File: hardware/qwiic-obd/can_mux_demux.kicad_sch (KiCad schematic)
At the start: 12 parts, among them Q201 2N7002, Q202 2N7002, Q203 2N7002, U201 TS5A3359DCUR, U202 TS5A3359DCUR, U203 TS5A3359DCUR

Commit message: Added initial layout (parts dump)
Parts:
- U201, U202, U203: footprint DCU8 -> UltraLibrarian:TS5A3359DCUR
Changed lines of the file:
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@@
       (effects (font (size 1.524 1.524)))
     )
-    (property "Footprint" "DCU8" (id 2) (at 105.41 125.984 0)
+    (property "Footprint" "UltraLibrarian:TS5A3359DCUR" (id 2) (at 105.41 125.984 0)
       (effects (font (size 1.524 1.524)) hide)
     )
@@
       (effects (font (size 1.524 1.524)))
     )
-    (property "Footprint" "DCU8" (id 2) (at 104.14 89.154 0)
+    (property "Footprint" "UltraLibrarian:TS5A3359DCUR" (id 2) (at 104.14 89.154 0)
       (effects (font (size 1.524 1.524)) hide)
     )
@@
       (effects (font (size 1.524 1.524)))
     )
-    (property "Footprint" "DCU8" (id 2) (at 104.14 54.864 0)
+    (property "Footprint" "UltraLibrarian:TS5A3359DCUR" (id 2) (at 104.14 54.864 0)
       (effects (font (size 1.524 1.524)) hide)
     )

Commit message: OK, layout v1 complete
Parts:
- added U202, U204: TS5A3359DCUR, UltraLibrarian:TS5A3359DCUR, symbol UltraLibrarian:TS5A3359DCUR
- renumbered U202 to U203, U203 to U205
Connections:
- net +5V: now also U202.8 (V+), U204.8 (V+)
- net CAN_SEL0: now also U202.6 (IN1), U204.6 (IN1)
- net CAN_SEL1: now also U202.5 (IN2), U204.5 (IN2)
- net GND: now also U202.4 (GND), U204.4 (GND)
- new net CAN_HI: U202.7 (COM)
- new net CAN_LO: U204.7 (COM)
- new net HS_CAN_HI: U202.1 (NO0)
- new net HS_CAN_LO: U204.1 (NO0)
- new net MS_CAN_HI: U202.2 (NO1)
- new net MS_CAN_LO: U204.2 (NO1)
- no-connect marks 1 -> 3
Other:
- moved on the sheet: Q201, Q202, Q203, R201, R202, R203, R204, R205, R206, U201, U203, U205

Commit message: Fix title block
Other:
- title: (none) -> QWIIC OBDII Interface
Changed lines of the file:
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@@
 (kicad_sch (version 20211123) (generator eeschema)
   (paper "A4")
+  (title_block
+    (title "QWIIC OBDII Interface")
+    (date "2023-01-03")
+  )
   (junction (at 140.97 135.89) (diameter 0) (color 0 0 0 0)
   )

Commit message: Shrunk layout a bit
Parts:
- U201, U202, U203, U204, U205: Digikey (none) -> 296-21193-1-ND
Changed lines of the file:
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@@
       (effects (font (size 1.524 1.524)))
+    )
+    (property "Digikey" "296-21193-1-ND" (id 4) (at 257.81 81.28 0)
+      (effects (font (size 1.27 1.27)) hide)
     )
     (pin "1")
@@
       (effects (font (size 1.524 1.524)))
     )
+    (property "Digikey" "296-21193-1-ND" (id 4) (at 257.81 115.57 0)
+      (effects (font (size 1.27 1.27)) hide)
+    )
     (pin "1")
     (pin "2")
@@
       (effects (font (size 1.524 1.524)))
     )
+    (property "Digikey" "296-21193-1-ND" (id 4) (at 99.06 135.89 0)
+      (effects (font (size 1.27 1.27)) hide)
+    )
     (pin "1")
     (pin "2")
@@
       (effects (font (size 1.524 1.524)))
     )
+    (property "Digikey" "296-21193-1-ND" (id 4) (at 97.79 99.06 0)
+      (effects (font (size 1.27 1.27)) hide)
+    )
     (pin "1")
     (pin "2")
@@
       (effects (font (size 1.524 1.524)))
     )
-    (pin "1")
+    (property "Digikey" "296-21193-1-ND" (id 4) (at 97.79 64.77 0)
+      (effects (font (size 1.27 1.27)) hide)
+    )
+    (pin "1")

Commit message: Switch out the PIC for an ATtiny424.
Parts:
- renumbered Q201 to Q1, Q202 to Q2, Q203 to Q3, R201 to R1, R203 to R2, R205 to R3, R202 to R4, R204 to R5, R206 to R6, U201 to U1, U203 to U2, U205 to U3, U202 to U4, U204 to U5
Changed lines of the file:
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@@
   (symbol (lib_id "power:+5V") (at 161.29 134.62 0) (unit 1)
     (in_bom yes) (on_board yes) (fields_autoplaced)
-    (property "Reference" "#PWR0209" (id 0) (at 161.29 138.43 0)
+    (property "Reference" "#PWR013" (id 0) (at 161.29 138.43 0)
       (effects (font (size 1.27 1.27)) hide)
     )
@@
   (symbol (lib_id "UltraLibrarian:TS5A3359DCUR") (at 257.81 81.28 0) (mirror y) (unit 1)
     (in_bom yes) (on_board yes) (fields_autoplaced)
-    (property "Reference" "U202" (id 0) (at 229.87 69.85 0)
+    (property "Reference" "U4" (id 0) (at 229.87 69.85 0)
       (effects (font (size 1.524 1.524)))
     )
@@
   (symbol (lib_id "power:+3V3") (at 140.97 66.04 0) (unit 1)
     (in_bom yes) (on_board yes) (fields_autoplaced)
-    (property "Reference" "#PWR0202" (id 0) (at 140.97 69.85 0)
+    (property "Reference" "#PWR08" (id 0) (at 140.97 69.85 0)
       (effects (font (size 1.27 1.27)) hide)
     )
@@
   (symbol (lib_id "power:+3V3") (at 140.97 99.06 0) (unit 1)
     (in_bom yes) (on_board yes) (fields_autoplaced)
-    (property "Reference" "#PWR0205" (id 0) (at 140.97 102.87 0)
+    (property "Reference" "#PWR09" (id 0) (at 140.97 102.87 0)
       (effects (font (size 1.27 1.27)) hide)
     )
@@
   (symbol (lib_id "power:+5V") (at 161.29 99.06 0) (unit 1)
     (in_bom yes) (on_board yes) (fields_autoplaced)
-    (property "Reference" "#PWR0206" (id 0) (at 161.29 102.87 0)
+    (property "Reference" "#PWR012" (id 0) (at 161.29 102.87 0)
       (effects (font (size 1.27 1.27)) hide)
     )
@@
   (symbol (lib_id "Device:R") (at 161.29 73.66 0) (unit 1)
     (in_bom yes) (on_board yes) (fields_autoplaced)
-    (property "Reference" "R202" (id 0) (at 163.83 72.3899 0)
+    (property "Reference" "R4" (id 0) (at 163.83 72.3899 0)
       (effects (font (size 1.27 1.27)) (justify left))
     )
@@
   (symbol (lib_id "Device:R") (at 161.29 142.24 0) (unit 1)
     (in_bom yes) (on_board yes) (fields_autoplaced)
-    (property "Reference" "R206" (id 0) (at 163.83 140.9699 0)
+    (property "Reference" "R6" (id 0) (at 163.83 140.9699 0)
       (effects (font (size 1.27 1.27)) (justify left))
     )
@@
   (symbol (lib_id "Device:R") (at 140.97 73.66 0) (unit 1)
     (in_bom yes) (on_board yes) (fields_autoplaced)
-    (property "Reference" "R201" (id 0) (at 143.51 72.3899 0)
+    (property "Reference" "R1" (id 0) (at 143.51 72.3899 0)
       (effects (font (size 1.27 1.27)) (justify left))
     )
@@
   (symbol (lib_id "Transistor_FET:2N7002") (at 152.4 77.47 270) (unit 1)
     (in_bom yes) (on_board yes) (fields_autoplaced)
-    (property "Reference" "Q201" (id 0) (at 152.4 85.09 90))
+    (property "Reference" "Q1" (id 0) (at 152.4 85.09 90))
     (property "Value" "2N7002" (id 1) (at 152.4 87.63 90))
     (property "Footprint" "Package_TO_SOT_SMD:SOT-23" (id 2) (at 150.495 82.55 0)
@@
   (symbol (lib_id "power:+3V3") (at 140.97 134.62 0) (unit 1)
     (in_bom yes) (on_board yes) (fields_autoplaced)
-    (property "Reference" "#PWR0208" (id 0) (at 140.97 138.43 0)
+    (property "Reference" "#PWR010" (id 0) (at 140.97 138.43 0)
       (effects (font (size 1.27 1.27)) hide)
     )
@@
   (symbol (lib_id "Device:R") (at 161.29 106.68 0) (unit 1)
     (in_bom yes) (on_board yes) (fields_autoplaced)
-    (property "Reference" "R204" (id 0) (at 163.83 105.4099 0)
+    (property "Reference" "R5" (id 0) (at 163.83 105.4099 0)
       (effects (font (size 1.27 1.27)) (justify left))
     )
@@
   (symbol (lib_id "UltraLibrarian:TS5A3359DCUR") (at 257.81 115.57 0) (mirror y) (unit 1)
     (in_bom yes) (on_board yes) (fields_autoplaced)
-    (property "Reference" "U204" (id 0) (at 229.87 104.14 0)
+    (property "Reference" "U5" (id 0) (at 229.87 104.14 0)
       (effects (font (size 1.524 1.524)))
     )
@@
   (symbol (lib_id "Transistor_FET:2N7002") (at 152.4 110.49 270) (unit 1)
     (in_bom yes) (on_board yes) (fields_autoplaced)
-    (property "Reference" "Q202" (id 0) (at 152.4 118.11 90))
+    (property "Reference" "Q2" (id 0) (at 152.4 118.11 90))
     (property "Value" "2N7002" (id 1) (at 152.4 120.65 90))
     (property "Footprint" "Package_TO_SOT_SMD:SOT-23" (id 2) (at 150.495 115.57 0)
@@
   (symbol (lib_id "Device:R") (at 140.97 106.68 0) (unit 1)
     (in_bom yes) (on_board yes) (fields_autoplaced)
-    (property "Reference" "R203" (id 0) (at 143.51 105.4099 0)
+    (property "Reference" "R2" (id 0) (at 143.51 105.4099 0)
       (effects (font (size 1.27 1.27)) (justify left))
     )
@@
   (symbol (lib_id "power:+3V3") (at 38.1 59.69 0) (mirror y) (unit 1)
     (in_bom yes) (on_board yes) (fields_autoplaced)
-    (property "Reference" "#PWR0201" (id 0) (at 38.1 63.5 0)
+    (property "Reference" "#PWR06" (id 0) (at 38.1 63.5 0)
       (effects (font (size 1.27 1.27)) hide)
     )
@@
   (symbol (lib_id "UltraLibrarian:TS5A3359DCUR") (at 99.06 135.89 0) (mirror y) (unit 1)
     (in_bom yes) (on_board yes) (fields_autoplaced)
-    (property "Reference" "U205" (id 0) (at 71.12 124.46 0)
+    (property "Reference" "U3" (id 0) (at 71.12 124.46 0)
       (effects (font (size 1.524 1.524)))
     )
@@
   (symbol (lib_id "power:+5V") (at 198.12 76.2 0) (unit 1)
     (in_bom yes) (on_board yes) (fields_autoplaced)
-    (property "Reference" "#PWR0204" (id 0) (at 198.12 80.01 0)
+    (property "Reference" "#PWR014" (id 0) (at 198.12 80.01 0)
       (effects (font (size 1.27 1.27)) hide)
     )
@@
   (symbol (lib_id "power:GND") (at 102.87 148.59 0) (mirror y) (unit 1)
     (in_bom yes) (on_board yes) (fields_autoplaced)
-    (property "Reference" "#PWR0210" (id 0) (at 102.87 154.94 0)
+    (property "Reference" "#PWR07" (id 0) (at 102.87 154.94 0)
       (effects (font (size 1.27 1.27)) hide)
     )
@@
   (symbol (lib_id "UltraLibrarian:TS5A3359DCUR") (at 97.79 99.06 0) (mirror y) (unit 1)
     (in_bom yes) (on_board yes) (fields_autoplaced)
-    (property "Reference" "U203" (id 0) (at 69.85 87.63 0)
+    (property "Reference" "U2" (id 0) (at 69.85 87.63 0)
       (effects (font (size 1.524 1.524)))
     )
@@
   (symbol (lib_id "UltraLibrarian:TS5A3359DCUR") (at 97.79 64.77 0) (mirror y) (unit 1)
     (in_bom yes) (on_board yes) (fields_autoplaced)
-    (property "Reference" "U201" (id 0) (at 69.85 53.34 0)
+    (property "Reference" "U1" (id 0) (at 69.85 53.34 0)
       (effects (font (size 1.524 1.524)))
     )
@@
   (symbol (lib_id "power:GND") (at 262.89 126.238 0) (mirror y) (unit 1)
     (in_bom yes) (on_board yes) (fields_autoplaced)
-    (property "Reference" "#PWR0207" (id 0) (at 262.89 132.588 0)
+    (property "Reference" "#PWR015" (id 0) (at 262.89 132.588 0)
       (effects (font (size 1.27 1.27)) hide)
     )
@@
   (symbol (lib_id "power:+5V") (at 161.29 66.04 0) (unit 1)
     (in_bom yes) (on_board yes) (fields_autoplaced)
-    (property "Reference" "#PWR0203" (id 0) (at 161.29 69.85 0)
+    (property "Reference" "#PWR011" (id 0) (at 161.29 69.85 0)
       (effects (font (size 1.27 1.27)) hide)
     )
@@
   (symbol (lib_id "Device:R") (at 140.97 142.24 0) (unit 1)
     (in_bom yes) (on_board yes) (fields_autoplaced)
-    (property "Reference" "R205" (id 0) (at 143.51 140.9699 0)
+    (property "Reference" "R3" (id 0) (at 143.51 140.9699 0)
       (effects (font (size 1.27 1.27)) (justify left))
     )
@@
   (symbol (lib_id "Transistor_FET:2N7002") (at 152.4 146.05 270) (unit 1)
     (in_bom yes) (on_board yes) (fields_autoplaced)
-    (property "Reference" "Q203" (id 0) (at 152.4 153.67 90))
+    (property "Reference" "Q3" (id 0) (at 152.4 153.67 90))
     (property "Value" "2N7002" (id 1) (at 152.4 156.21 90))
     (property "Footprint" "Package_TO_SOT_SMD:SOT-23" (id 2) (at 150.495 151.13 0)

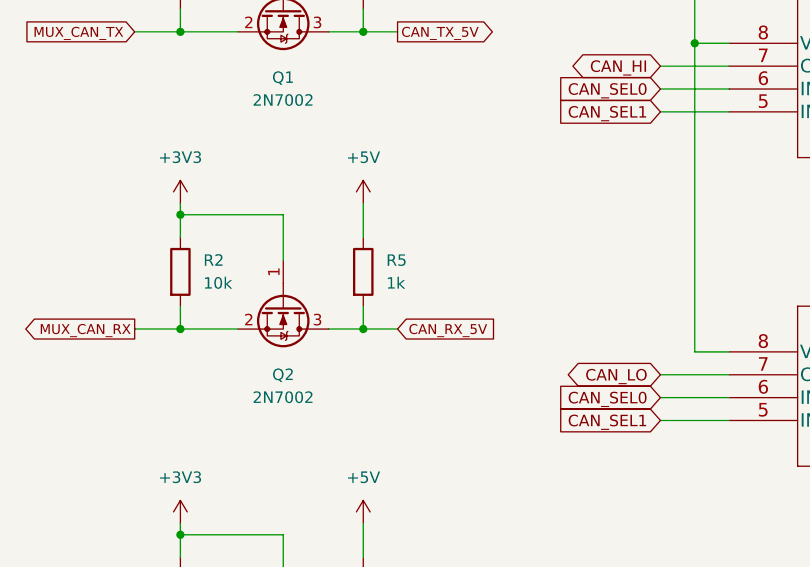
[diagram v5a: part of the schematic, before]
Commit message: Moved git libs to new repo
- https://github.com/Beirdo/KiCad-Git-Libraries
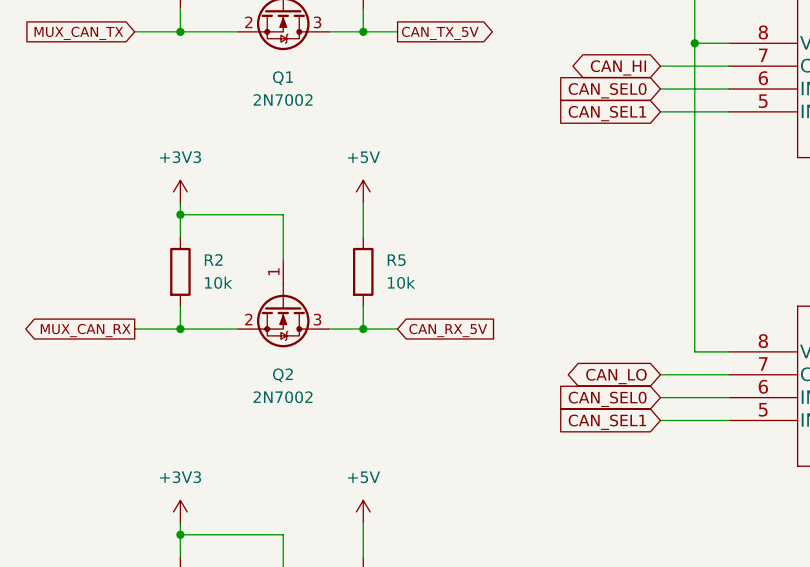
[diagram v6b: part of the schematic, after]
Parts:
- R5: value 1k -> 10k
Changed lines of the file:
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@@
       (effects (font (size 1.27 1.27)) (justify left))
     )
-    (property "Value" "1k" (id 1) (at 163.83 107.9499 0)
+    (property "Value" "10k" (id 1) (at 163.83 107.9499 0)
       (effects (font (size 1.27 1.27)) (justify left))
     )
